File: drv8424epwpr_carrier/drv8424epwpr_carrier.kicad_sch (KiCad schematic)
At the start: 5 parts, among them J4 Conn_01x08, J5 Conn_01x08, U1 DRV8424EPWPR, U2 DMP4013LFG-7

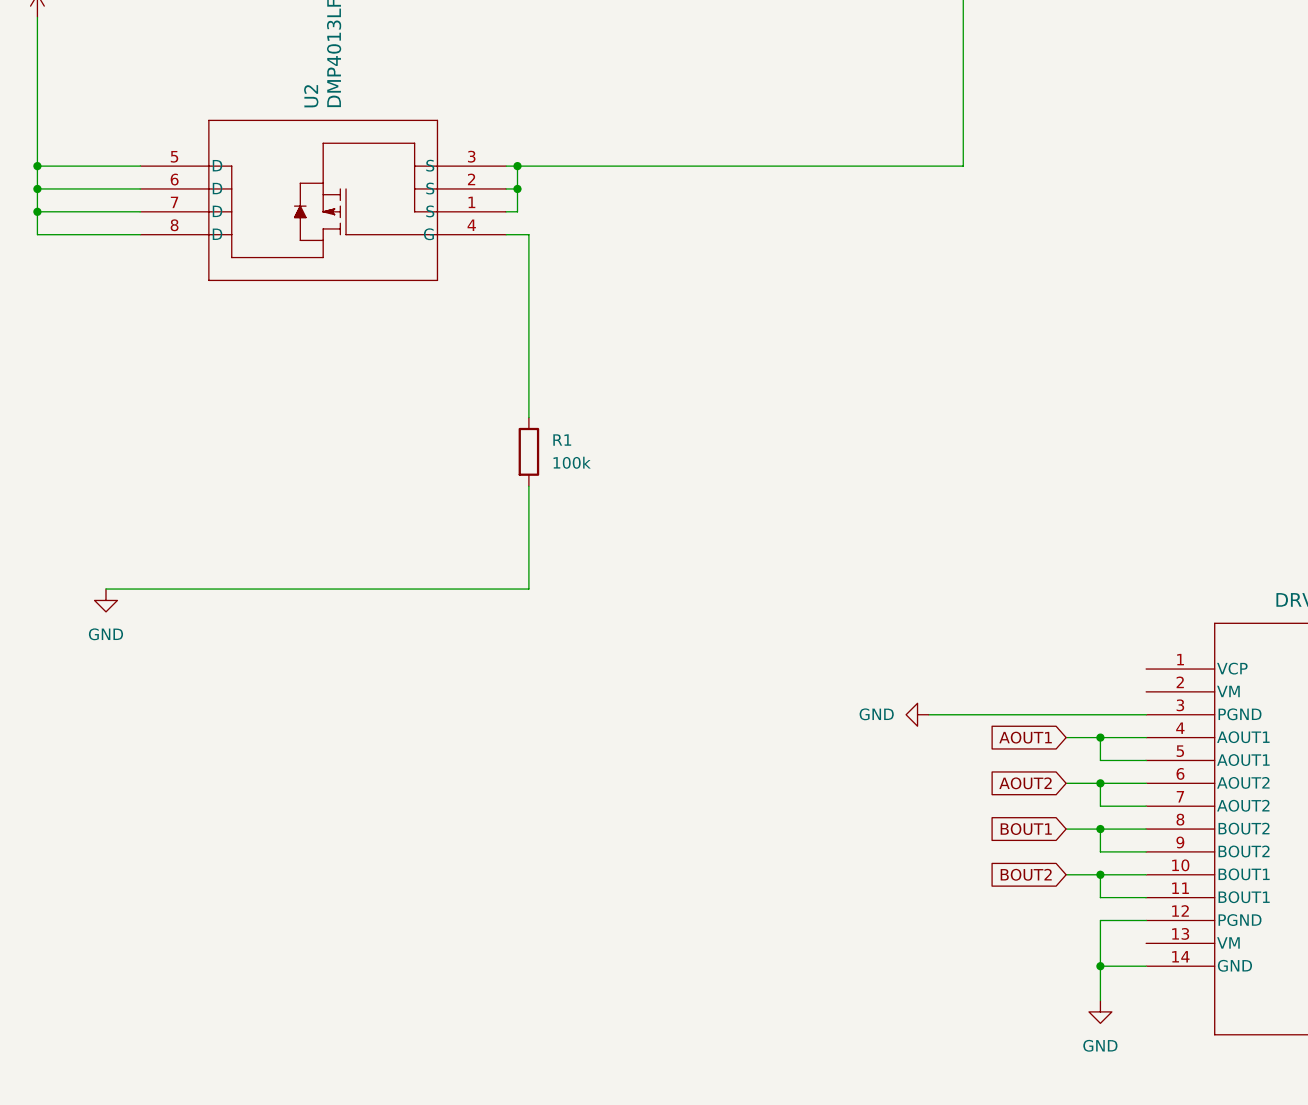
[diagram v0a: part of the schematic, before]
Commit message: add reverse protection circuit
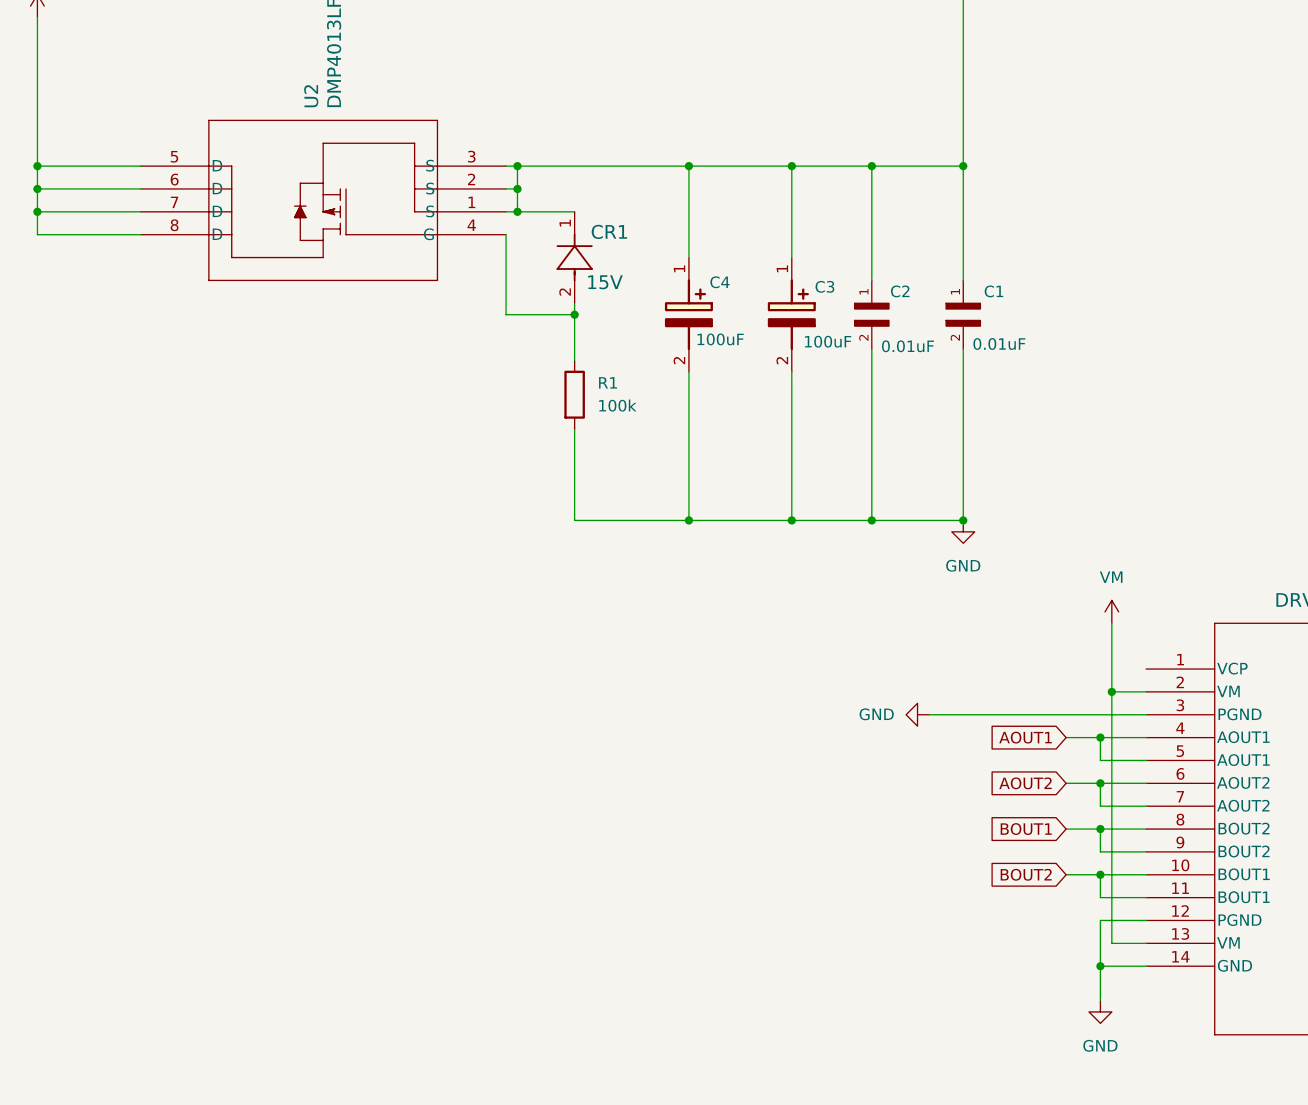
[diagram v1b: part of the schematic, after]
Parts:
- added C1, C2: 0.01uF, CGA2B3X7R1V103K050BB:CAPC1005X55N, symbol CGA2B3X7R1V103K050BB:CGA2B3X7R1V103K050BB
- added C3, C4: 100uF, EEE0GA101SR, symbol EEE-1AA101WR:EEE-1AA101WR
- added CR1: 15V, SOD123_DIO, symbol MMSZ5245B-7-F:MMSZ5245B-7-F
- R1: footprint (none) -> Resistor_SMD:R_1206_3216Metric
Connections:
- net GND: now also C1.2, C2.2, C3.2 (-), C4.2 (-)
- net VM: now also U1.13 (VM), U1.2 (VM), C1.1, C2.1, C3.1 (+), C4.1 (+), CR1.1
- net at R1.1, U2.4 (G): now also CR1.2
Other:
- moved on the sheet: R1

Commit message: update schematic
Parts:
- removed C1, C2: 0.01uF, CGA2B3X7R1V103K050BB:CAPC1005X55N, symbol CGA2B3X7R1V103K050BB:CGA2B3X7R1V103K050BB
- added C_DVDD: 1uF, GRM319R71A105KA01D:CAPC3216X95N, symbol GRM319R71A105KA01D:GRM319R71A105KA01D
- added C_SW: 0.022uF, CAPC340180_88N_KEM, symbol C1206C223J8RACTU:C1206C223J8RACTU
- added C_VCP: 0.22uF, CAPC340180_100N_KEM, symbol C1206C224K4RACTU:C1206C224K4RACTU
- added C_VM1, C_VM2: 0.01uF, CAPC220145_88N_KEM, symbol C0805C103K8RACTU:C0805C103K8RACTU
- renumbered C3 to C_VM3, C4 to C_VM4
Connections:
- net GND: now also C_DVDD.2, C_VM1.2, C_VM2.2
- net VM: now also C_VCP.2, C_VM1.1, C_VM2.1
- net at U1.1 (VCP): now also C_VCP.1
- net DVDD: now reaches U1.15 (DVDD)
- net DVDD: now also C_DVDD.1
- net at U1.27 (CPL): now also C_SW.2
- net at U1.28 (CPH): now also C_SW.1

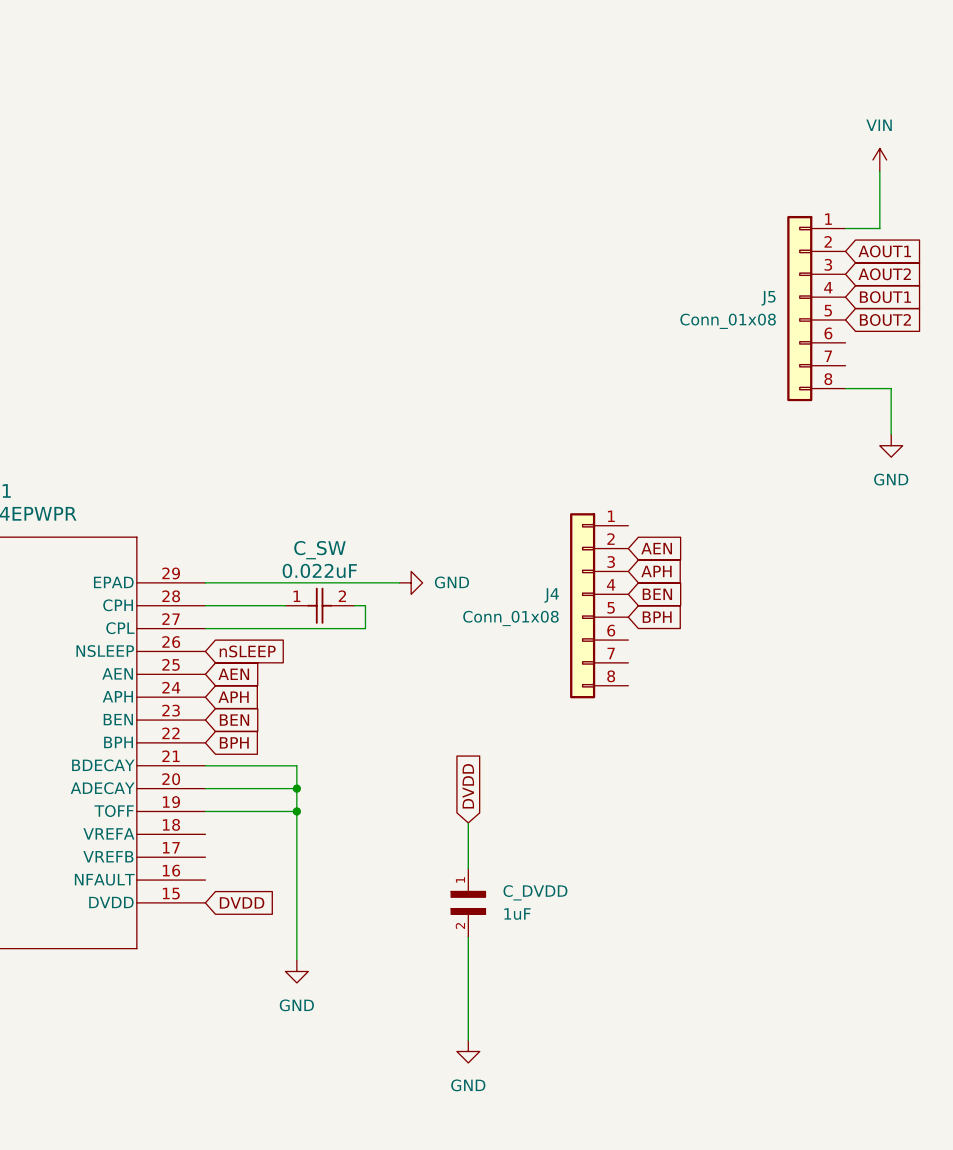
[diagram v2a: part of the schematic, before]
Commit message: update current regulation circuit
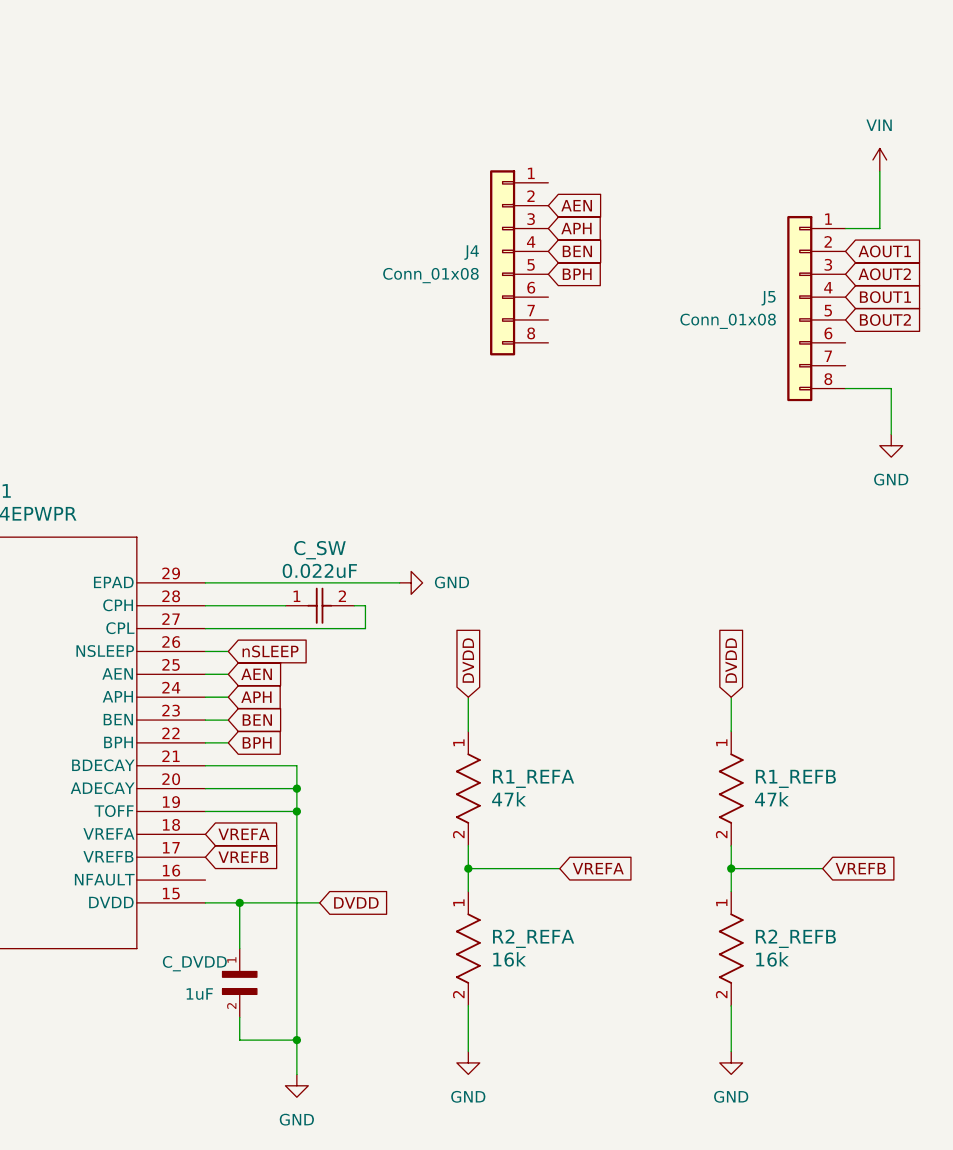
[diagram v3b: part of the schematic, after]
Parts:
- added R1_REFA, R1_REFB: 47k, RC1206N_YAG, symbol RC1206FR-0747KL:RC1206FR-0747KL
- added R2_REFA, R2_REFB: 16k, RC1206N_YAG, symbol RC1206FR-0716KL:RC1206FR-0716KL
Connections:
- net DVDD: now also R1_REFA.1, R1_REFB.1
- net GND: now also R2_REFA.2, R2_REFB.2
- net VREFB: now reaches U1.17 (VREFB)
- net VREFB: now also R1_REFB.2, R2_REFB.1
- net VREFA: now reaches U1.18 (VREFA)
- net VREFA: now also R1_REFA.2, R2_REFA.1
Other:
- moved on the sheet: C_DVDD, J4

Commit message: finish schematic
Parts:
- removed R1: 100k, Resistor_SMD:R_1206_3216Metric, symbol Device:R
- added R1: 100k, RC1206N_YAG, symbol RC1206FR-07100KL:RC1206FR-07100KL
- added R_nFAULT: 10k, RC1206N_YAG, symbol RC1206FR-0710KL:RC1206FR-0710KL
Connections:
- net nSLEEP is gone; now on net NSLEEP: U1.26 (NSLEEP)
- net AEN: now also J4.3 (Pin_3); no longer J4.2 (Pin_2)
- net AOUT1: now also J5.1 (Pin_1); no longer J5.2 (Pin_2)
- net AOUT2: now also J5.2 (Pin_2); no longer J5.3 (Pin_3)
- net APH: now also J4.4 (Pin_4); no longer J4.3 (Pin_3)
- net BEN: now also J4.5 (Pin_5); no longer J4.4 (Pin_4)
- net BOUT1: now also J5.6 (Pin_6); no longer J5.4 (Pin_4)
- net BPH: now also J4.6 (Pin_6); no longer J4.5 (Pin_5)
- net GND: now also J4.2 (Pin_2), J5.4 (Pin_4), J5.7 (Pin_7), R1.2; no longer J5.8 (Pin_8)
- net VIN: now also J5.3 (Pin_3); no longer J5.1 (Pin_1)
- net VM: now also J4.1 (Pin_1)
- net NFAULT: now reaches J4.7 (Pin_7)
- net NFAULT: now also U1.16 (NFAULT), R_nFAULT.2
- net NSLEEP: now reaches J4.8 (Pin_8)
- net at CR1.2, U2.4 (G): now also R1.1
- new net +3V3: J5.8 (Pin_8), R_nFAULT.1
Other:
- moved on the sheet: C_VM1, C_VM2, C_VM3, C_VM4, J4, J5, R1_REFA, R1_REFB, R2_REFA, R2_REFB

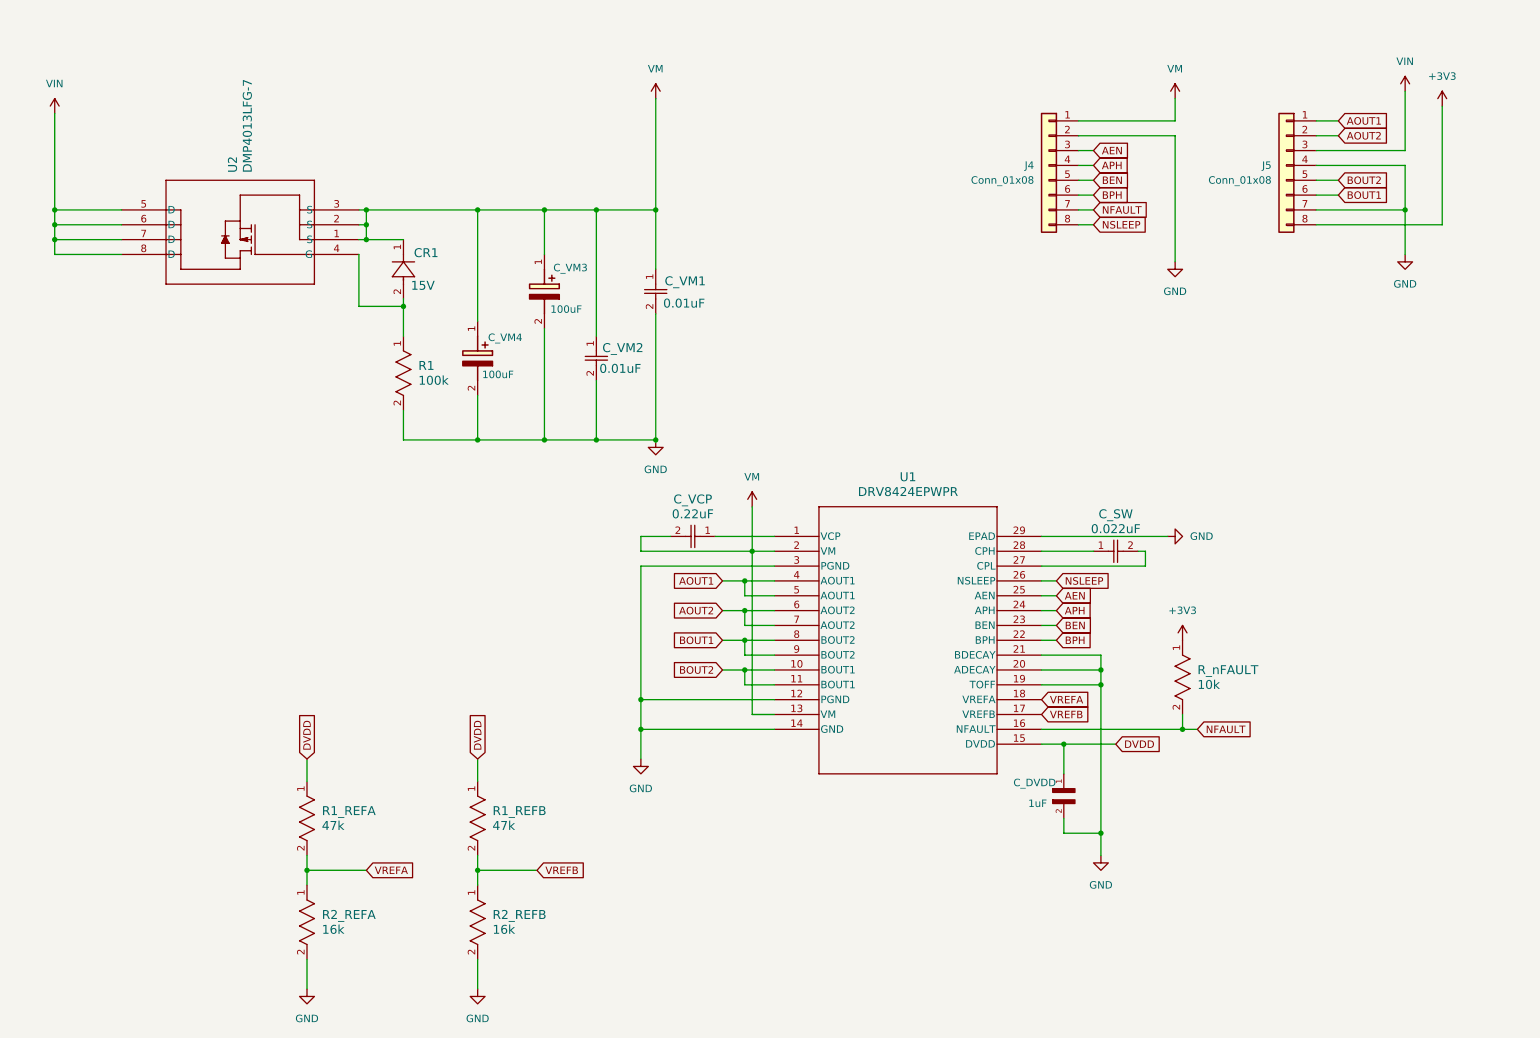
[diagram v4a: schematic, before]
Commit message: add motor dir indication LEDs
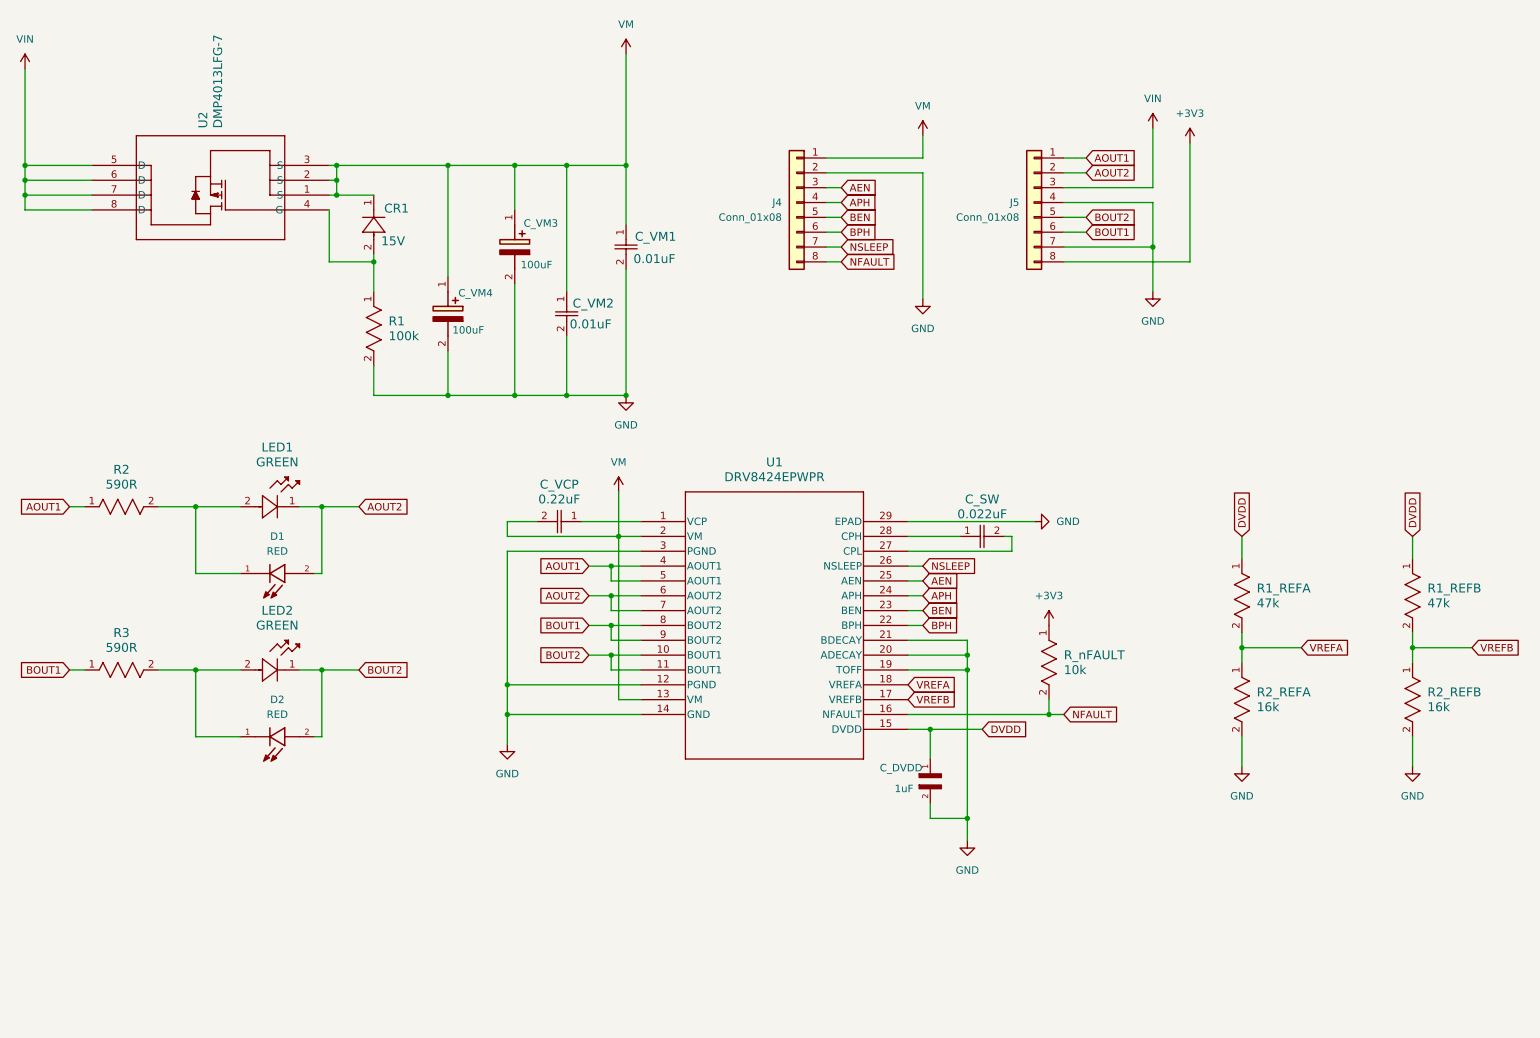
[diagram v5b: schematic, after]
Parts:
- added D1, D2: RED, APHCM2012SURCK-F01:LED_APHCM2012SURCK-F01, symbol APHCM2012SURCK-F01:APHCM2012SURCK-F01
- added LED1, LED2: GREEN, LED_APHCM2012CGCK-F01_KNB, symbol APHCM2012CGCK-F01:APHCM2012CGCK-F01
- added R2, R3: 590R, RC1206N_YAG, symbol RC1206FR-07590RL:RC1206FR-07590RL
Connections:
- net AOUT1: now also R2.1
- net AOUT2: now also D1.2, LED1.1
- net BOUT1: now also R3.1
- net BOUT2: now also D2.2, LED2.1
- net NFAULT: now also J4.8 (Pin_8); no longer J4.7 (Pin_7)
- net NSLEEP: now also J4.7 (Pin_7); no longer J4.8 (Pin_8)
- new net: D2.1, LED2.2, R3.2
- new net: D1.1, LED1.2, R2.2
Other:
- moved on the sheet: CR1, C_DVDD, C_SW, C_VCP, C_VM1, C_VM2, C_VM3, C_VM4, J4, J5, R1, R1_REFA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

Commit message: add power indication LED
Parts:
- added LED1: YELLOW, APHCM2012SYCK-F01:LED_APHCM2012SYCK-F01, symbol APHCM2012SYCK-F01:APHCM2012SYCK-F01
- added R4: 590R, RC1206N_YAG, symbol RC1206FR-07590RL:RC1206FR-07590RL
- renumbered LED1 to LED2, D1 to LED3, LED2 to LED4, D2 to LED5
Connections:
- net GND: now also R4.2
- net VM: now also LED1.2
- new net: LED1.1, R4.1
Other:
- title: (none) -> 6V Motor Driver Carrier
- moved on the sheet: J4, J5
